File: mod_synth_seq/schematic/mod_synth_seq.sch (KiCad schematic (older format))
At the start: 66 parts

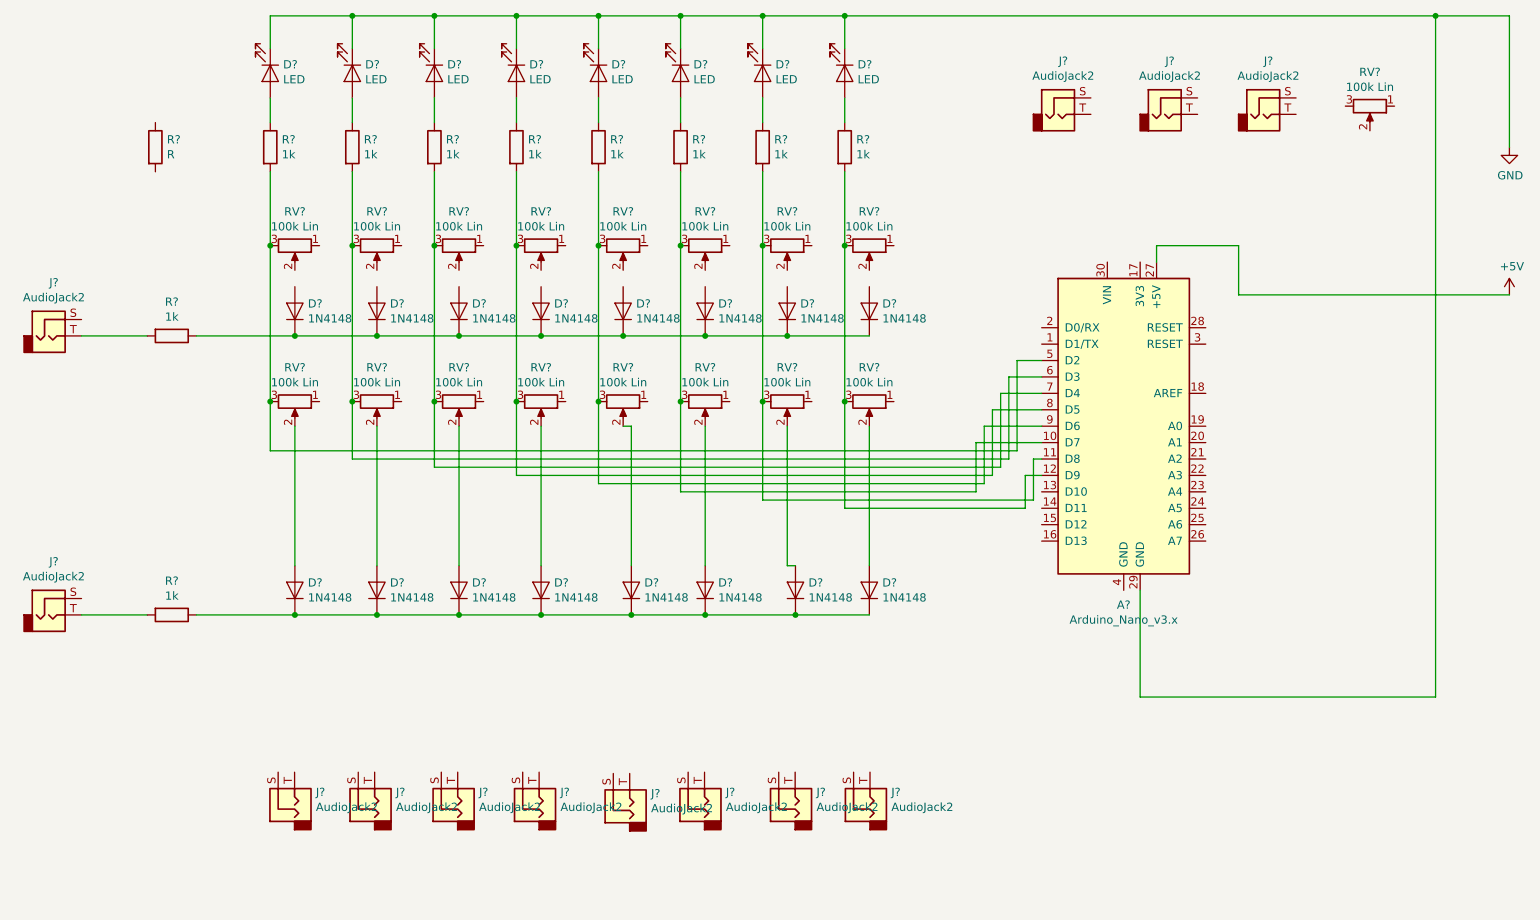
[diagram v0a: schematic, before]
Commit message: Finish schematic for seq and add schematic for clk
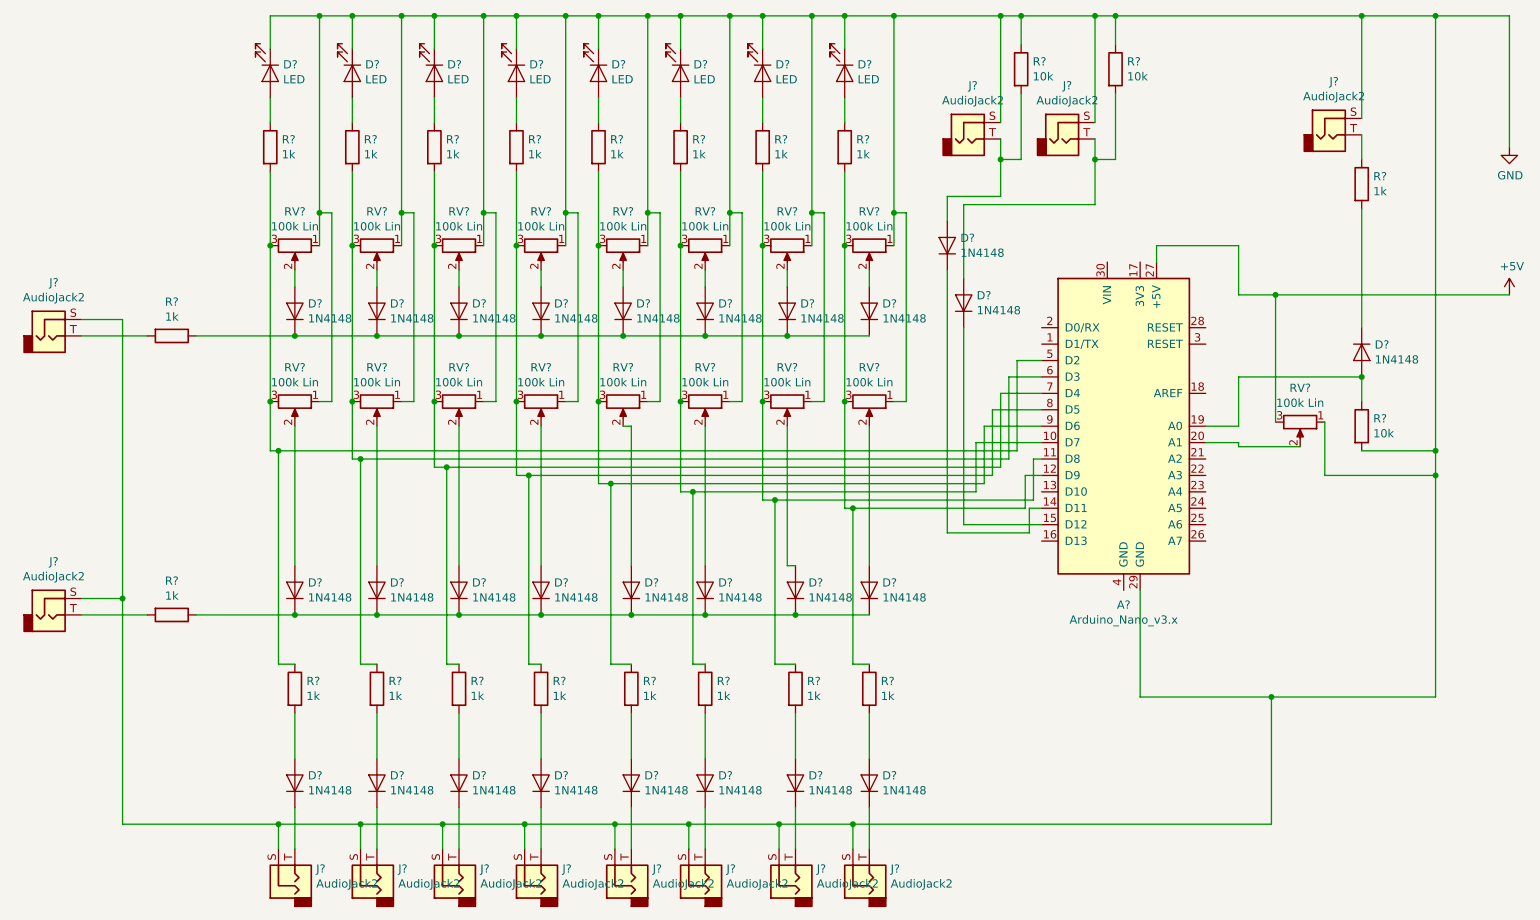
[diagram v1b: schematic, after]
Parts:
- added D? (x11): 1N4148, Diode_THT:D_DO-35_SOD27_P7.62mm_Horizontal, symbol Diode:1N4148
- added R? (x3): 10k, symbol Device:R
- added R? (x8): 1k, symbol Device:R
- R?: value R -> 1k
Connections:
- net +5V: now also RV?.3
- net GND: now also J?.S, J?.S, J?.S, J?.S, J?.S, J?.S, J?.S, J?.S, J?.S, J?.S, J?.S, J?.S, J?.S, RV?.1, RV?.1, RV?.1, RV?.1, RV?.1, RV?.1, RV?.1, RV?.1, RV?.1, RV?.1, RV?.1, RV?.1, RV?.1, RV?.1, RV?.1, RV?.1, RV?.1, R?.1, R?.1, R?.2
- net at D?.2 (A): now also RV?.2
- net at A?.5 (D2), R?.2, RV?.3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: now also R?.1
- net at R?.2: now also D?.2 (A)
- net at A?.10 (D7), R?.2, RV?.3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: now also R?.1
- net at A?.11 (D8), R?.2, RV?.3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: now also R?.1
- net at A?.12 (D9), R?.2, RV?.3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: now also R?.1
- net at A?.14 (D11): now also D?.1 (K)
- net at A?.15 (D12): now also D?.1 (K)
- net at A?.19 (A0): now also D?.2 (A), R?.1
- net at A?.20 (A1): now also RV?.2
- net at A?.6 (D3), R?.2, RV?.3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: now also R?.1
- net at A?.7 (D4), R?.2, RV?.3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: now also R?.1
- net at A?.8 (D5), R?.2, RV?.3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: now also R?.1
- net at A?.9 (D6), R?.2, RV?.3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: now also R?.1
- net at RV?.2: now also D?.2 (A) (x7)
- net at J?.T: now also D?.2 (A), R?.2 (x2)
- net at J?.T: now also R?.1
- net at J?.T: now also D?.1 (K) (x8)
- new net: D?.1 (K), R?.2
- new net: D?.2 (A), R?.2 (x7)
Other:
- moved on the sheet: J?, R?, RV?

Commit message: Remove pull-down resistor from gate output
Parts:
- removed R?: 10k, symbol Device:R
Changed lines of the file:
@@
 	9350 1875 9350 2600
-$Comp
-L Device:R R?
-U 1 1 5D29C94C
-P 9350 3200
-F 0 "R?" H 9420 3246 50  0000 L CNN
-F 1 "10k" H 9420 3155 50  0000 L CNN
-F 2 "" V 9280 3200 50  0001 C CNN
-F 3 "~" H 9350 3200 50  0001 C CNN
-	1    9350 3200
-	1    0    0    -1
-$EndComp
-Wire Wire Line
-	9350 2900 9350 3050
-Connection ~ 9350 2900
-Wire Wire Line
-	9350 3350 9800 3350
-Connection ~ 9800 3350
-Wire Wire Line
-	9800 3350 9800 700
 $Comp
 L Diode:1N4148 D?
@@
 Connection ~ 9800 3500
 Wire Wire Line
-	9800 3500 9800 3350
-Wire Wire Line
 	1550 2550 1800 2550
 Wire Wire Line
@@
 Wire Wire Line
 	6500 1900 6500 700
+Wire Wire Line
+	9800 700  9800 3500
 $EndSCHEMATC

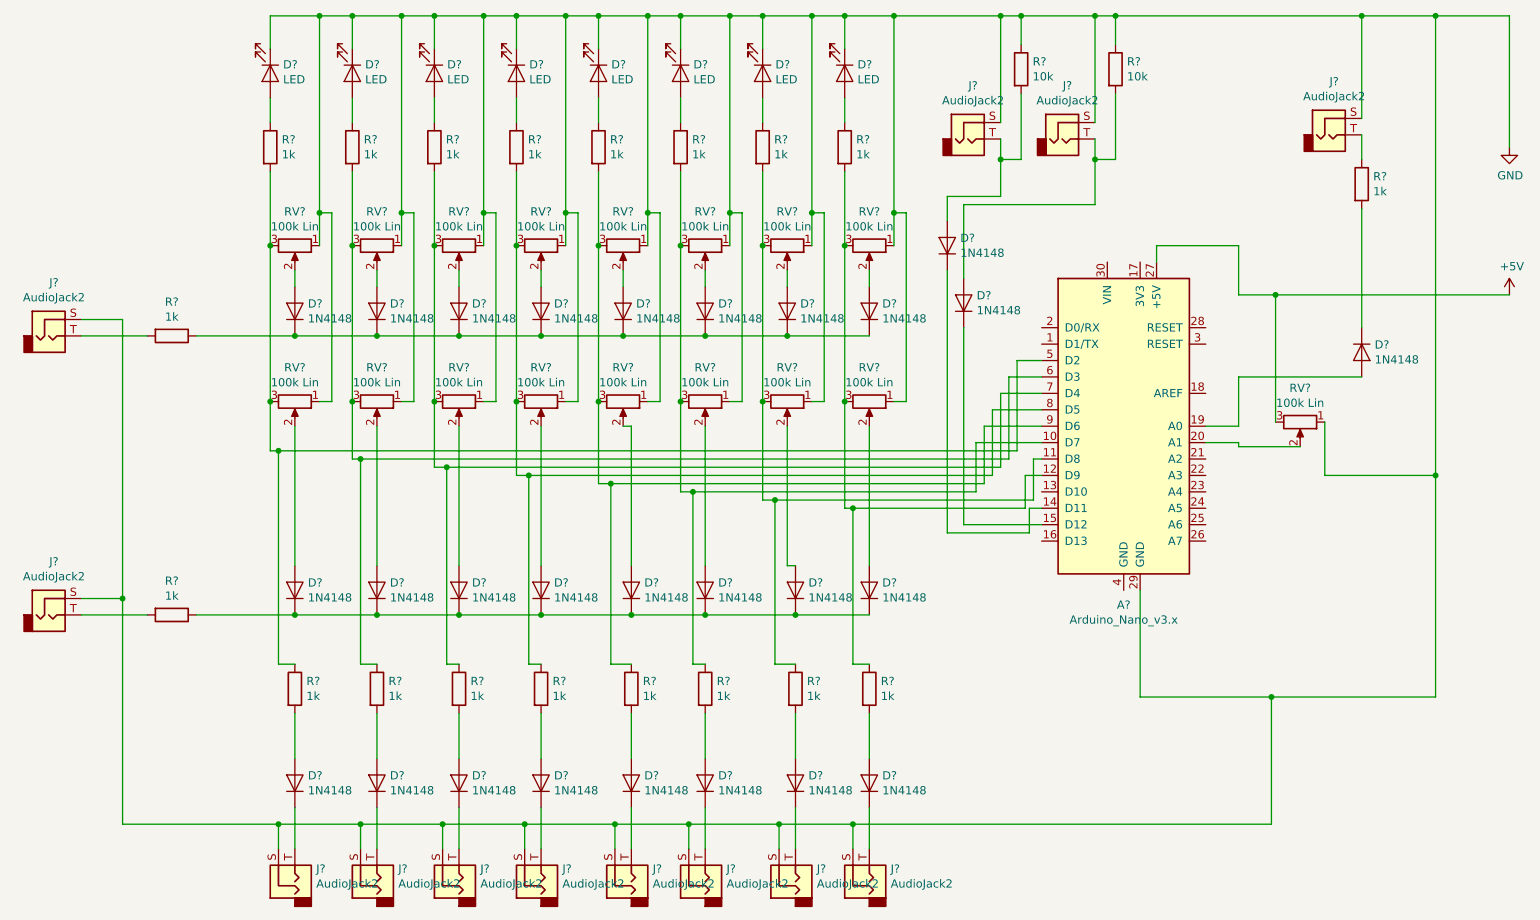
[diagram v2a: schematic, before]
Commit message: Add labels and cleanup square/PWM section
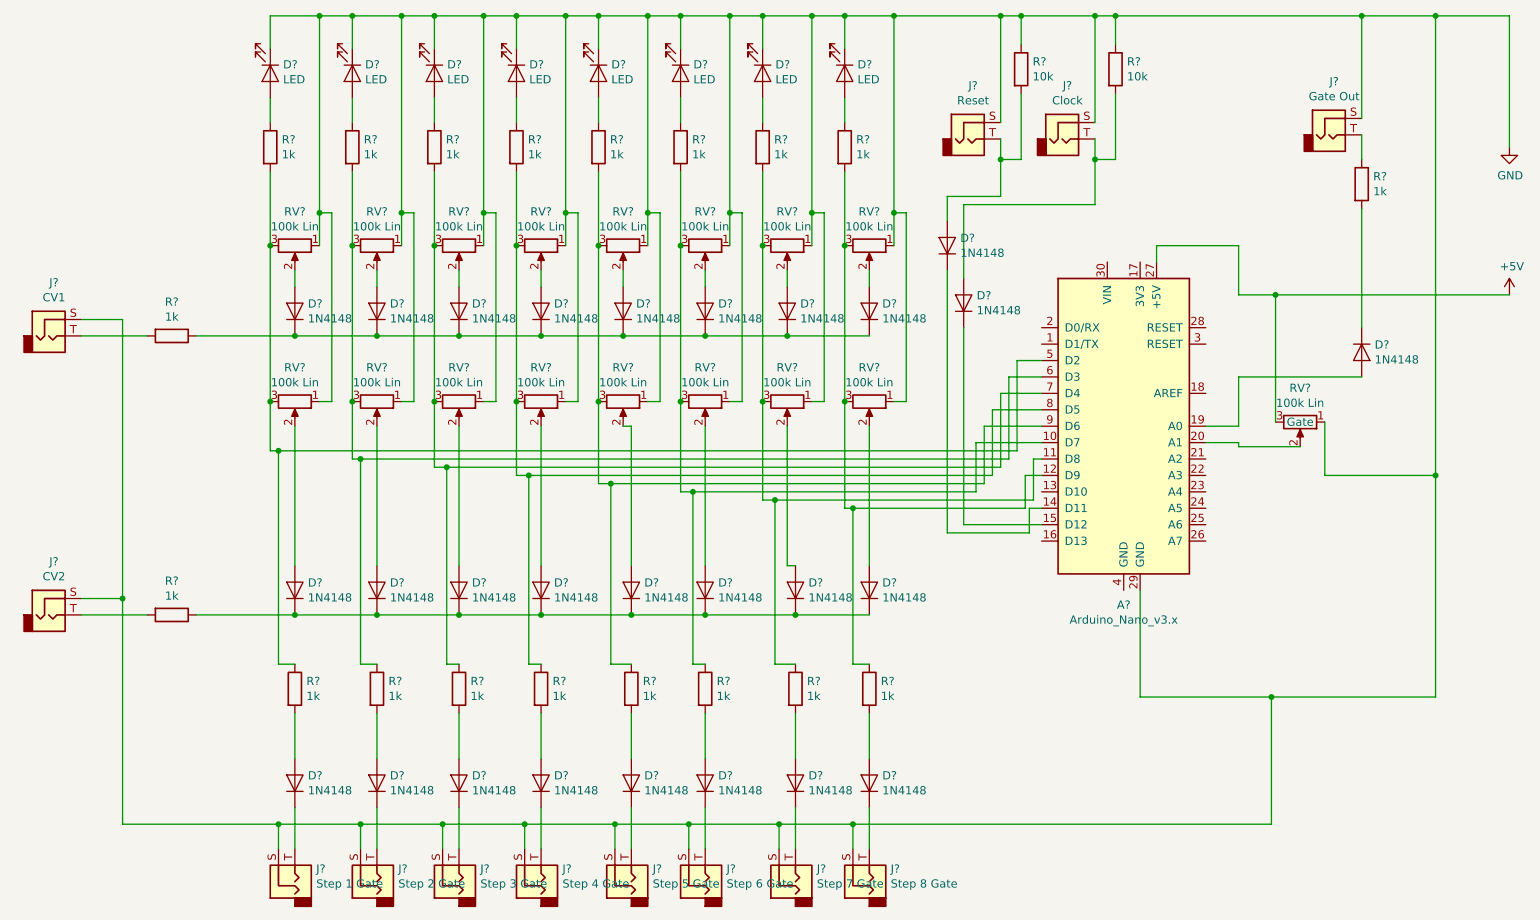
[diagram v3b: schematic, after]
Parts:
- J?: value AudioJack2 -> CV1
- J?: value AudioJack2 -> CV2
- J?: value AudioJack2 -> Reset
- J?: value AudioJack2 -> Clock
- J?: value AudioJack2 -> Gate Out
- J?: value AudioJack2 -> Step 1 Gate
- J?: value AudioJack2 -> Step 2 Gate
- J?: value AudioJack2 -> Step 3 Gate
- J?: value AudioJack2 -> Step 4 Gate
- J?: value AudioJack2 -> Step 5 Gate
- J?: value AudioJack2 -> Step 6 Gate
- J?: value AudioJack2 -> Step 7 Gate
- J?: value AudioJack2 -> Step 8 Gate
- RV?: Text (none) -> Gate
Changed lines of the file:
@@
 P 1350 2650
 F 0 "J?" H 1382 2975 50  0000 C CNN
-F 1 "AudioJack2" H 1382 2884 50  0000 C CNN
+F 1 "CV1" H 1382 2884 50  0000 C CNN
 F 2 "" H 1350 2650 50  0001 C CNN
 F 3 "~" H 1350 2650 50  0001 C CNN
@@
 P 1350 4350
 F 0 "J?" H 1382 4675 50  0000 C CNN
-F 1 "AudioJack2" H 1382 4584 50  0000 C CNN
+F 1 "CV2" H 1382 4584 50  0000 C CNN
 F 2 "" H 1350 4350 50  0001 C CNN
 F 3 "~" H 1350 4350 50  0001 C CNN
@@
 P 6950 1450
 F 0 "J?" H 6982 1775 50  0000 C CNN
-F 1 "AudioJack2" H 6982 1684 50  0000 C CNN
+F 1 "Reset" H 6982 1684 50  0000 C CNN
 F 2 "" H 6950 1450 50  0001 C CNN
 F 3 "~" H 6950 1450 50  0001 C CNN
@@
 P 7525 1450
 F 0 "J?" H 7557 1775 50  0000 C CNN
-F 1 "AudioJack2" H 7557 1684 50  0000 C CNN
+F 1 "Clock" H 7557 1684 50  0000 C CNN
 F 2 "" H 7525 1450 50  0001 C CNN
 F 3 "~" H 7525 1450 50  0001 C CNN
@@
 P 9150 1425
 F 0 "J?" H 9182 1750 50  0000 C CNN
-F 1 "AudioJack2" H 9182 1659 50  0000 C CNN
+F 1 "Gate Out" H 9182 1659 50  0000 C CNN
 F 2 "" H 9150 1425 50  0001 C CNN
 F 3 "~" H 9150 1425 50  0001 C CNN
@@
 F 2 "" H 8975 3175 50  0001 C CNN
 F 3 "~" H 8975 3175 50  0001 C CNN
+F 4 "Gate" V 8975 3175 50  0000 C CNN "Text"
 	1    8975 3175
 	0    1    1    0
@@
 P 2850 5975
 F 0 "J?" V 2928 5845 50  0000 R CNN
-F 1 "AudioJack2" V 2837 5845 50  0000 R CNN
+F 1 "Step 1 Gate" V 2837 5845 50  0000 R CNN
 F 2 "" H 2850 5975 50  0001 C CNN
 F 3 "~" H 2850 5975 50  0001 C CNN
@@
 P 3350 5975
 F 0 "J?" V 3428 5845 50  0000 R CNN
-F 1 "AudioJack2" V 3337 5845 50  0000 R CNN
+F 1 "Step 2 Gate" V 3337 5845 50  0000 R CNN
 F 2 "" H 3350 5975 50  0001 C CNN
 F 3 "~" H 3350 5975 50  0001 C CNN
@@
 P 3850 5975
 F 0 "J?" V 3928 5845 50  0000 R CNN
-F 1 "AudioJack2" V 3837 5845 50  0000 R CNN
+F 1 "Step 3 Gate" V 3837 5845 50  0000 R CNN
 F 2 "" H 3850 5975 50  0001 C CNN
 F 3 "~" H 3850 5975 50  0001 C CNN
@@
 P 4350 5975
 F 0 "J?" V 4428 5845 50  0000 R CNN
-F 1 "AudioJack2" V 4337 5845 50  0000 R CNN
+F 1 "Step 4 Gate" V 4337 5845 50  0000 R CNN
 F 2 "" H 4350 5975 50  0001 C CNN
 F 3 "~" H 4350 5975 50  0001 C CNN
@@
 P 4900 5975
 F 0 "J?" V 4978 5845 50  0000 R CNN
-F 1 "AudioJack2" V 4887 5845 50  0000 R CNN
+F 1 "Step 5 Gate" V 4887 5845 50  0000 R CNN
 F 2 "" H 4900 5975 50  0001 C CNN
 F 3 "~" H 4900 5975 50  0001 C CNN
@@
 P 5350 5975
 F 0 "J?" V 5428 5845 50  0000 R CNN
-F 1 "AudioJack2" V 5337 5845 50  0000 R CNN
+F 1 "Step 6 Gate" V 5337 5845 50  0000 R CNN
 F 2 "" H 5350 5975 50  0001 C CNN
 F 3 "~" H 5350 5975 50  0001 C CNN
@@
 P 6350 5975
 F 0 "J?" V 6428 5845 50  0000 R CNN
-F 1 "AudioJack2" V 6337 5845 50  0000 R CNN
+F 1 "Step 8 Gate" V 6337 5845 50  0000 R CNN
 F 2 "" H 6350 5975 50  0001 C CNN
 F 3 "~" H 6350 5975 50  0001 C CNN
@@
 P 5900 5975
 F 0 "J?" V 5978 5845 50  0000 R CNN
-F 1 "AudioJack2" V 5887 5845 50  0000 R CNN
+F 1 "Step 7 Gate" V 5887 5845 50  0000 R CNN
 F 2 "" H 5900 5975 50  0001 C CNN
 F 3 "~" H 5900 5975 50  0001 C CNN

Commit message: Add footprints to seq for AlphPot and EurorackJack
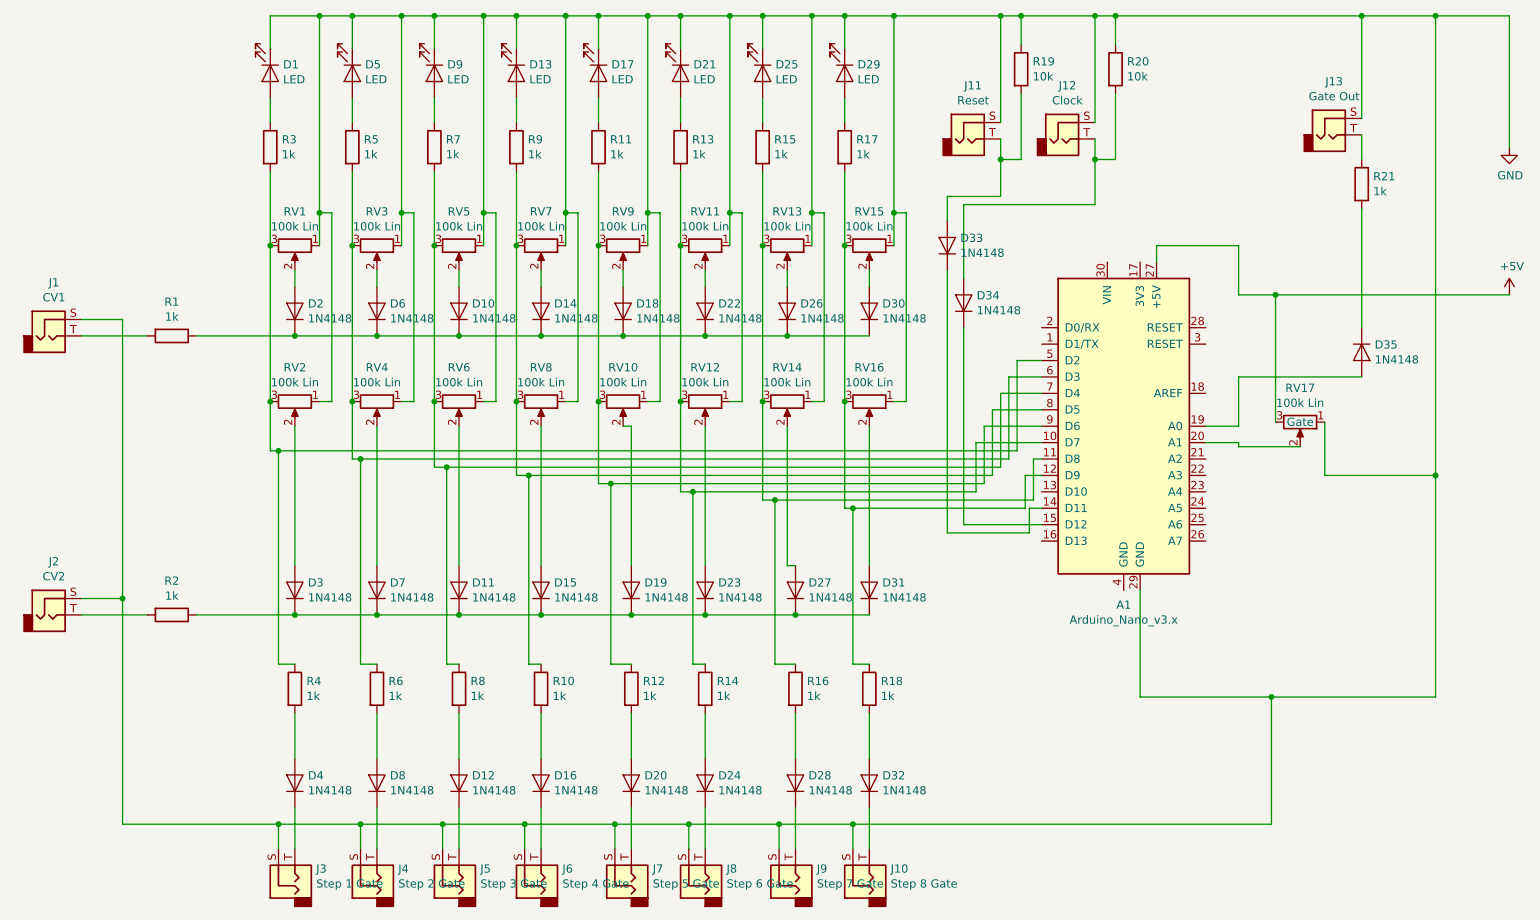
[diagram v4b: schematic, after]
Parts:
- D1, D13, D17, D21, D25, D29, D5, D9: renamed from D?; footprint (none) -> LED_THT:LED_D5.0mm
- J1, J10, J11, J12, J13, J2, J3, J4, J5, J6, J7, J8, J9: renamed from J?; footprint (none) -> Connector_Audio:Jack_3.5mm_QingPu_WQP-PJ398SM_Vertical_CircularHoles
- R1, R10, R11, R12, R13, R14, R15, R16, R17, R18, R19, R2, R20, R21, R3, R4, R5, R6, R7, R8, R9: renamed from R?; footprint (none) -> Resistor_THT:R_Axial_DIN0207_L6.3mm_D2.5mm_P10.16mm_Horizontal
- RV1, RV10, RV11, RV12, RV13, RV14, RV15, RV16, RV17, RV2, RV3, RV4, RV5, RV6, RV7, RV8, RV9: renamed from RV?; footprint (none) -> Potentiometer_THT:Potentiometer_Alpha_RD901F-40-00D_Single_Vertical
- gave numbers to parts that had none: 28
